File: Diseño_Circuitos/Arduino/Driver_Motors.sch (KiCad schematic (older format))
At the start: 22 parts, among them J10 Conn_01x02, J9 Conn_01x02, Q1 MMBT3904, Q2 MMBT3904, Q3 MMBT3904, Q4 MMBT3904, Q5 MMBT3904, Q6 MMBT3904, U5 L293DD

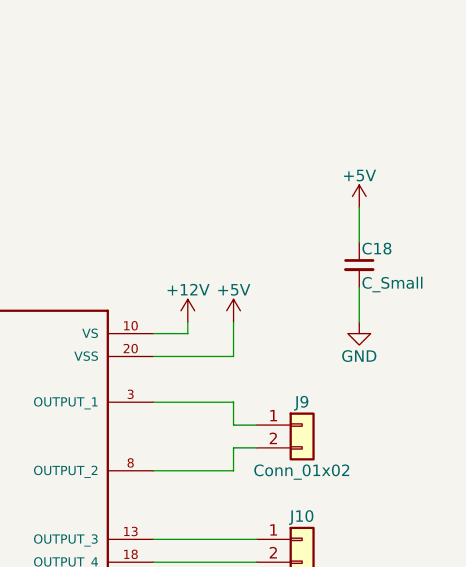
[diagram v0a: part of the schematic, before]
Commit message: pcb components placed
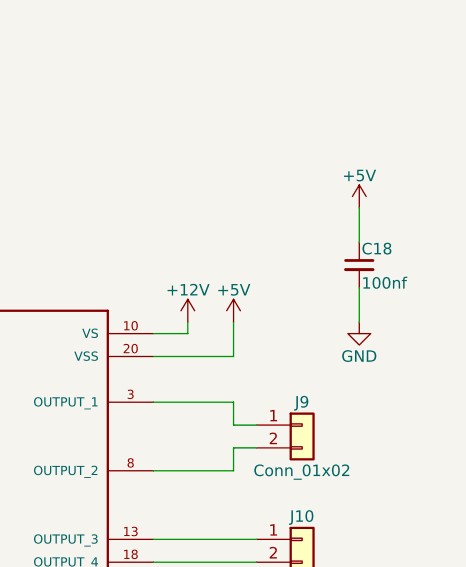
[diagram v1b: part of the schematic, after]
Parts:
- C18: value C_Small -> 100nf; footprint (none) -> custom footprints:C_0805_HandSoldering
- J10, J9: footprint (none) -> custom footprints:Pin_Header_Straight_1x02_Pitch2.54mm
- Q1, Q2, Q3, Q4, Q5, Q6: footprint TO_SOT_Packages_SMD:SOT-23 -> custom footprints:SOT-23
- R25, R26, R27, R28, R29, R30, R31, R32, R33, R34, R35, R36: footprint (none) -> custom footprints:R_0805_HandSoldering
- U5: footprint SOIC127P1032X265-20N -> custom footprints:SOIC127P1032X265-20N
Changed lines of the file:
@@
 F 0 "Q1" H 2850 2025 50  0000 L CNN
 F 1 "MMBT3904" H 2850 1950 50  0000 L CNN
-F 2 "TO_SOT_Packages_SMD:SOT-23" H 2850 1875 50  0001 L CIN
+F 2 "custom footprints:SOT-23" H 2850 1875 50  0001 L CIN
 F 3 "" H 2650 1950 50  0001 L CNN
 	1    2650 1950
@@
 F 0 "R27" H 2780 2370 50  0000 L CNN
 F 1 "10K" H 2780 2310 50  0000 L CNN
-F 2 "" H 2750 2350 50  0000 C CNN
+F 2 "custom footprints:R_0805_HandSoldering" H 2750 2350 50  0001 C CNN
 F 3 "" H 2750 2350 50  0000 C CNN
 	1    2750 2350
@@
 F 0 "R25" H 2230 1970 50  0000 L CNN
 F 1 "1K" H 2230 1910 50  0000 L CNN
-F 2 "" H 2200 1950 50  0000 C CNN
+F 2 "custom footprints:R_0805_HandSoldering" H 2200 1950 50  0001 C CNN
 F 3 "" H 2200 1950 50  0000 C CNN
 	1    2200 1950
@@
 F 0 "Q2" H 4650 2025 50  0000 L CNN
 F 1 "MMBT3904" H 4650 1950 50  0000 L CNN
-F 2 "TO_SOT_Packages_SMD:SOT-23" H 4650 1875 50  0001 L CIN
+F 2 "custom footprints:SOT-23" H 4650 1875 50  0001 L CIN
 F 3 "" H 4450 1950 50  0001 L CNN
 	1    4450 1950
@@
 F 0 "R28" H 4580 2370 50  0000 L CNN
 F 1 "10K" H 4580 2310 50  0000 L CNN
-F 2 "" H 4550 2350 50  0000 C CNN
+F 2 "custom footprints:R_0805_HandSoldering" H 4550 2350 50  0001 C CNN
 F 3 "" H 4550 2350 50  0000 C CNN
 	1    4550 2350
@@
 F 0 "R26" H 4030 1970 50  0000 L CNN
 F 1 "1K" H 4030 1910 50  0000 L CNN
-F 2 "" H 4000 1950 50  0000 C CNN
+F 2 "custom footprints:R_0805_HandSoldering" H 4000 1950 50  0001 C CNN
 F 3 "" H 4000 1950 50  0000 C CNN
 	1    4000 1950
@@
 F 0 "Q3" H 2850 3575 50  0000 L CNN
 F 1 "MMBT3904" H 2850 3500 50  0000 L CNN
-F 2 "TO_SOT_Packages_SMD:SOT-23" H 2850 3425 50  0001 L CIN
+F 2 "custom footprints:SOT-23" H 2850 3425 50  0001 L CIN
 F 3 "" H 2650 3500 50  0001 L CNN
 	1    2650 3500
@@
 F 0 "R31" H 2780 3920 50  0000 L CNN
 F 1 "10K" H 2780 3860 50  0000 L CNN
-F 2 "" H 2750 3900 50  0000 C CNN
+F 2 "custom footprints:R_0805_HandSoldering" H 2750 3900 50  0001 C CNN
 F 3 "" H 2750 3900 50  0000 C CNN
 	1    2750 3900
@@
 F 0 "Q4" H 4650 3575 50  0000 L CNN
 F 1 "MMBT3904" H 4650 3500 50  0000 L CNN
-F 2 "TO_SOT_Packages_SMD:SOT-23" H 4650 3425 50  0001 L CIN
+F 2 "custom footprints:SOT-23" H 4650 3425 50  0001 L CIN
 F 3 "" H 4450 3500 50  0001 L CNN
 	1    4450 3500
@@
 F 0 "R32" H 4580 3920 50  0000 L CNN
 F 1 "10K" H 4580 3860 50  0000 L CNN
-F 2 "" H 4550 3900 50  0000 C CNN
+F 2 "custom footprints:R_0805_HandSoldering" H 4550 3900 50  0001 C CNN
 F 3 "" H 4550 3900 50  0000 C CNN
 	1    4550 3900
@@
 F 0 "R30" H 4030 3520 50  0000 L CNN
 F 1 "1K" H 4030 3460 50  0000 L CNN
-F 2 "" H 4000 3500 50  0000 C CNN
+F 2 "custom footprints:R_0805_HandSoldering" H 4000 3500 50  0001 C CNN
 F 3 "" H 4000 3500 50  0000 C CNN
 	1    4000 3500
@@
 F 0 "Q5" H 2850 5075 50  0000 L CNN
 F 1 "MMBT3904" H 2850 5000 50  0000 L CNN
-F 2 "TO_SOT_Packages_SMD:SOT-23" H 2850 4925 50  0001 L CIN
+F 2 "custom footprints:SOT-23" H 2850 4925 50  0001 L CIN
 F 3 "" H 2650 5000 50  0001 L CNN
 	1    2650 5000
@@
 F 0 "R35" H 2780 5420 50  0000 L CNN
 F 1 "10K" H 2780 5360 50  0000 L CNN
-F 2 "" H 2750 5400 50  0000 C CNN
+F 2 "custom footprints:R_0805_HandSoldering" H 2750 5400 50  0001 C CNN
 F 3 "" H 2750 5400 50  0000 C CNN
 	1    2750 5400
@@
 F 0 "Q6" H 4650 5075 50  0000 L CNN
 F 1 "MMBT3904" H 4650 5000 50  0000 L CNN
-F 2 "TO_SOT_Packages_SMD:SOT-23" H 4650 4925 50  0001 L CIN
+F 2 "custom footprints:SOT-23" H 4650 4925 50  0001 L CIN
 F 3 "" H 4450 5000 50  0001 L CNN
 	1    4450 5000
@@
 F 0 "R36" H 4580 5420 50  0000 L CNN
 F 1 "10K" H 4580 5360 50  0000 L CNN
-F 2 "" H 4550 5400 50  0000 C CNN
+F 2 "custom footprints:R_0805_HandSoldering" H 4550 5400 50  0001 C CNN
 F 3 "" H 4550 5400 50  0000 C CNN
 	1    4550 5400
@@
 F 0 "R34" H 4030 5020 50  0000 L CNN
 F 1 "1K" H 4030 4960 50  0000 L CNN
-F 2 "" H 4000 5000 50  0000 C CNN
+F 2 "custom footprints:R_0805_HandSoldering" H 4000 5000 50  0001 C CNN
 F 3 "" H 4000 5000 50  0000 C CNN
 	1    4000 5000
@@
 F 0 "R29" H 2230 3520 50  0000 L CNN
 F 1 "1K" H 2230 3460 50  0000 L CNN
-F 2 "" H 2200 3500 50  0000 C CNN
+F 2 "custom footprints:R_0805_HandSoldering" H 2200 3500 50  0001 C CNN
 F 3 "" H 2200 3500 50  0000 C CNN
 	1    2200 3500
@@
 F 0 "R33" H 2230 5020 50  0000 L CNN
 F 1 "1K" H 2230 4960 50  0000 L CNN
-F 2 "" H 2200 5000 50  0000 C CNN
+F 2 "custom footprints:R_0805_HandSoldering" H 2200 5000 50  0001 C CNN
 F 3 "" H 2200 5000 50  0000 C CNN
 	1    2200 5000
@@
 F 0 "U5" H 6259 4336 50  0000 L BNN
 F 1 "L293DD" H 6259 2813 50  0000 L BNN
-F 2 "SOIC127P1032X265-20N" H 6850 3600 50  0001 L BNN
+F 2 "custom footprints:SOIC127P1032X265-20N" H 6850 3600 50  0001 L BNN
 F 3 "STMicroelectronics" H 6850 3600 50  0001 L BNN
 F 4 "IPC-7351B" H 6850 3600 50  0001 L BNN "Campo4"
@@
 F 0 "J10" H 8300 4000 50  0000 C CNN
 F 1 "Conn_01x02" H 8300 3700 50  0000 C CNN
-F 2 "" H 8300 3900 50  0001 C CNN
+F 2 "custom footprints:Pin_Header_Straight_1x02_Pitch2.54mm" H 8300 3900 50  0001 C CNN
 F 3 "" H 8300 3900 50  0001 C CNN
 	1    8300 3900
@@
 F 0 "J9" H 8300 3500 50  0000 C CNN
 F 1 "Conn_01x02" H 8300 3200 50  0000 C CNN
-F 2 "" H 8300 3400 50  0001 C CNN
+F 2 "custom footprints:Pin_Header_Straight_1x02_Pitch2.54mm" H 8300 3400 50  0001 C CNN
 F 3 "" H 8300 3400 50  0001 C CNN
 	1    8300 3400
@@
 P 8550 2700
 F 0 "C18" H 8560 2770 50  0000 L CNN
-F 1 "C_Small" H 8560 2620 50  0000 L CNN
-F 2 "" H 8550 2700 50  0000 C CNN
+F 1 "100nf" H 8560 2620 50  0000 L CNN
+F 2 "custom footprints:C_0805_HandSoldering" H 8550 2700 50  0001 C CNN
 F 3 "" H 8550 2700 50  0000 C CNN
 	1    8550 2700
